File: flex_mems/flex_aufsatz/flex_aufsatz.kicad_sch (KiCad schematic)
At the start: 0 parts

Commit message: flex header first steps
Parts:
- added C6: 2.2uF, Capacitor_SMD:C_0402_1005Metric, symbol Device:C_Small
- added IC1: ADPL44002AUJZ-1.8-R7, ADPL44002AUJZ-1.8:SOT95P280X100-5N, symbol ADPL44002AUJZ-1.8:ADPL44002AUJZ-1.8-R7
- added J1, J2: Conn_01x22_Socket, Connector_PinSocket_2.54mm:PinSocket_1x22_P2.54mm_Vertical, symbol Connector:Conn_01x22_Socket
- added J3, J4: 10164228-0101A1RLF, header:AMPHENOL_10164228-0101A1RLF, symbol header:10164228-0101A1RLF
- added U1: ADAU7118ACPZRL, CP-16-22_ADI, symbol mux:ADAU7118ACPZRL
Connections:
- new net +1V8: C6.2, IC1.4 (SENSE/ADJ), IC1.5 (VOUT), U1.14 (DVDD)
- new net +3.3V: IC1.1 (VIN), IC1.3 (EN), J1.1 (Pin_1), U1.13 (EN), U1.16 (IOVDD)
- new net +3V3: J3.1, J4.1
- new net GND: C6.1, IC1.2 (GND), J1.22 (Pin_22), J3.10, J4.10, U1.15 (GND), U1.7 (SCL), U1.8 (SDA)
- new net MIC_CLK: J3.5, J4.4
- new net MIC_DOUT_0: J3.9
- new net MIC_DOUT_1: J3.7
- new net MIC_DOUT_2: J4.8
- no-connect marks 0 -> 11

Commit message: Schematics done
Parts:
- added C1, C2: 100nF, Capacitor_SMD:C_0402_1005Metric, symbol Device:C_Small
- added C3, C4: 2.2uF, Capacitor_SMD:C_0402_1005Metric, symbol Device:C_Small
- U1: footprint CP-16-22_ADI -> mux:QFN50P300X300X80-17N-D
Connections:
- net +3.3V: now also C1.1, C2.1, C3.1, C4.1
- net GND: now also J2.1 (Pin_1), U1.17 (EPAD), C1.2, C2.2, C3.2, C4.2
- net MIC_DOUT_0: now also U1.2 (PDM_DAT0)
- net MIC_DOUT_1: now also U1.3 (PDM_DAT1)
- net MIC_DOUT_2: now also U1.5 (PDM_DAT2)
- net TDM_DATA: now reaches J1.18 (Pin_18)
- net TDM_DATA: now also U1.11 (SDATA)
- net WS: now reaches J1.4 (Pin_4)
- net WS: now also U1.9 (FSYNC)
- net BCLK: now reaches J1.5 (Pin_5)
- net BCLK: now also U1.10 (BCLK)
- net MIC_CLK0: now reaches U1.1 (PDM_CLK0)
- net MIC_CLK0: now also J3.5
- net MIC_CLK1: now reaches U1.4 (PDM_CLK1)
- net MIC_CLK1: now also J4.4
- removed net MIC_CLK: J3.5, J4.4
- no-connect marks 11 -> 51

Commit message: flex_aufsatz1.0
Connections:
- net +3V3 is gone; now on net +3.3V: J3.1, J4.1
- net +3.3V: now also J1.2 (Pin_2)
- net GND: now also J2.21 (Pin_21), J2.22 (Pin_22)
- no-connect marks 51 -> 48
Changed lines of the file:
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@@
 	)
 	(junction
+		(at 35.56 29.21)
+		(diameter 0)
+		(color 0 0 0 0)
+	)
+	(junction
 		(at 266.7 44.45)
 		(diameter 0)
@@
 		(color 0 0 0 0)
 	)
+	(junction
+		(at 64.77 82.55)
+		(diameter 0)
+		(color 0 0 0 0)
+	)
 	(no_connect
 		(at 68.58 41.91)
@@
 	)
 	(no_connect
-		(at 68.58 82.55)
-	)
-	(no_connect
 		(at 68.58 67.31)
 	)
@@
 	)
 	(no_connect
-		(at 40.64 31.75)
-	)
-	(no_connect
 		(at 68.58 49.53)
 	)
@@
 	)
 	(no_connect
-		(at 68.58 80.01)
-	)
-	(no_connect
 		(at 68.58 62.23)
 	)
@@
 	(wire
 		(pts
+			(xy 64.77 82.55) (xy 68.58 82.55)
+		)
+		(stroke
+			(width 0)
+			(type default)
+		)
+	)
+	(wire
+		(pts
 			(xy 40.64 82.55) (xy 33.02 82.55)
 		)
@@
 	(wire
 		(pts
-			(xy 29.21 29.21) (xy 40.64 29.21)
+			(xy 29.21 29.21) (xy 35.56 29.21)
 		)
 		(stroke
@@
 	(wire
 		(pts
+			(xy 64.77 86.36) (xy 64.77 82.55)
+		)
+		(stroke
+			(width 0)
+			(type default)
+		)
+	)
+	(wire
+		(pts
 			(xy 274.32 44.45) (xy 274.32 49.53)
 		)
@@
 	(wire
 		(pts
+			(xy 64.77 80.01) (xy 64.77 82.55)
+		)
+		(stroke
+			(width 0)
+			(type default)
+		)
+	)
+	(wire
+		(pts
 			(xy 193.04 111.76) (xy 193.04 104.14)
 		)
@@
 	(wire
 		(pts
+			(xy 35.56 31.75) (xy 35.56 29.21)
+		)
+		(stroke
+			(width 0)
+			(type default)
+		)
+	)
+	(wire
+		(pts
 			(xy 81.28 119.38) (xy 90.17 119.38)
 		)
@@
 	(wire
 		(pts
+			(xy 40.64 31.75) (xy 35.56 31.75)
+		)
+		(stroke
+			(width 0)
+			(type default)
+		)
+	)
+	(wire
+		(pts
 			(xy 199.39 146.05) (xy 195.58 146.05)
 		)
@@
 	(wire
 		(pts
+			(xy 35.56 29.21) (xy 40.64 29.21)
+		)
+		(stroke
+			(width 0)
+			(type default)
+		)
+	)
+	(wire
+		(pts
 			(xy 90.17 127) (xy 90.17 129.54)
 		)
@@
 	(wire
 		(pts
+			(xy 68.58 80.01) (xy 64.77 80.01)
+		)
+		(stroke
+			(width 0)
+			(type default)
+		)
+	)
+	(wire
+		(pts
 			(xy 270.51 40.64) (xy 270.51 44.45)
 		)
@@
 	)
 	(symbol
+		(lib_id "power:GND")
+		(at 64.77 86.36 0)
+		(unit 1)
+		(exclude_from_sim no)
+		(in_bom yes)
+		(on_board yes)
+		(dnp no)
+		(fields_autoplaced yes)
+		(property "Reference" "#PWR015"
+			(at 64.77 92.71 0)
+			(effects
+				(font
+					(size 1.27 1.27)
+				)
+				(hide yes)
+			)
+		)
+		(property "Value" "GND"
+			(at 64.77 91.44 0)
+			(effects
+				(font
+					(size 1.27 1.27)
+				)
+			)
+		)
+		(property "Footprint" ""
+			(at 64.77 86.36 0)
+			(effects
+				(font
+					(size 1.27 1.27)
+				)
+				(hide yes)
+			)
+		)
+		(property "Datasheet" ""
+			(at 64.77 86.36 0)
+			(effects
+				(font
+					(size 1.27 1.27)
+				)
+				(hide yes)
+			)
+		)
+		(property "Description" "Power symbol creates a global label with name \"GND\" , ground"
+			(at 64.77 86.36 0)
+			(effects
+				(font
+					(size 1.27 1.27)
+				)
+				(hide yes)
+			)
+		)
+		(pin "1"
+		)
+		(instances
+			(project "flex_aufsatz"
+				(path "/1aeb6fc2-022e-4961-b0a7-a22f4026d221"
+					(reference "#PWR015")
+					(unit 1)
+				)
+			)
+		)
+	)
+	(symbol
 		(lib_id "Device:C_Small")
 		(at 26.67 25.4 270)
@@
 			)
 		)
-		(property "Value" "+3V3"
+		(property "Value" "+3.3V"
 			(at 193.04 100.33 0)
 			(effects
@@
 			)
 		)
-		(property "Value" "+3V3"
+		(property "Value" "+3.3V"
 			(at 195.58 134.62 0)
 			(effects

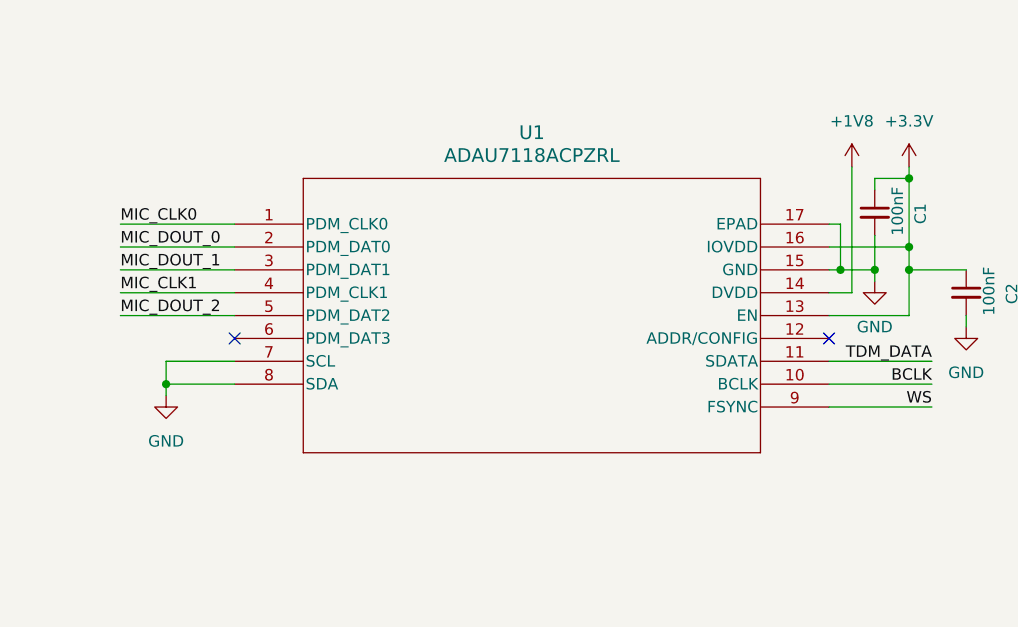
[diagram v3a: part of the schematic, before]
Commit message: GND zone update
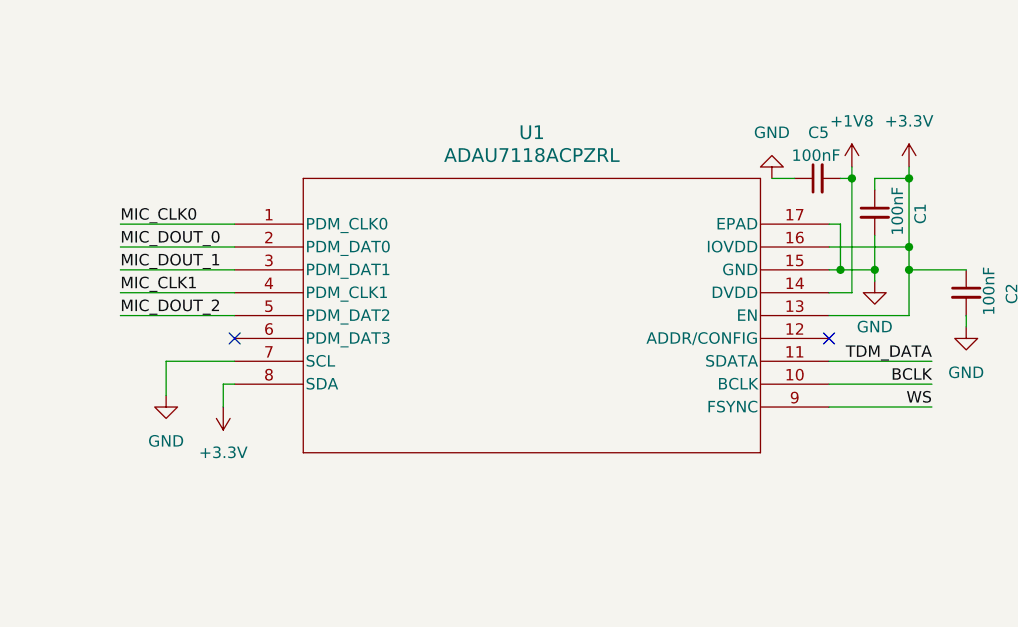
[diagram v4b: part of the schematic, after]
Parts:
- added C5: 100nF, Capacitor_SMD:C_0402_1005Metric, symbol Device:C_Small
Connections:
- net +1V8: now also C5.2
- net +3.3V: now also U1.8 (SDA)
- net GND: now also C5.1; no longer U1.8 (SDA)
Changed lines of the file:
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@@
 	)
 	(junction
-		(at 90.17 119.38)
+		(at 267.97 34.29)
 		(diameter 0)
 		(color 0 0 0 0)
 	)
 	(junction
-		(at 191.77 57.15)
+		(at 90.17 119.38)
 		(diameter 0)
 		(color 0 0 0 0)
@@
 	(wire
 		(pts
-			(xy 191.77 54.61) (xy 191.77 57.15)
+			(xy 186.69 39.37) (xy 199.39 39.37)
 		)
 		(stroke
@@
 	(wire
 		(pts
-			(xy 186.69 39.37) (xy 199.39 39.37)
+			(xy 64.77 82.55) (xy 68.58 82.55)
 		)
 		(stroke
@@
 	(wire
 		(pts
-			(xy 64.77 82.55) (xy 68.58 82.55)
+			(xy 40.64 82.55) (xy 33.02 82.55)
 		)
 		(stroke
@@
 	(wire
 		(pts
-			(xy 40.64 82.55) (xy 33.02 82.55)
+			(xy 265.43 39.37) (xy 266.7 39.37)
 		)
 		(stroke
@@
 	(wire
 		(pts
-			(xy 265.43 39.37) (xy 266.7 39.37)
+			(xy 224.79 148.59) (xy 236.22 148.59)
 		)
 		(stroke
@@
 	(wire
 		(pts
-			(xy 224.79 148.59) (xy 236.22 148.59)
+			(xy 199.39 57.15) (xy 198.12 57.15)
 		)
 		(stroke
@@
 	(wire
 		(pts
+			(xy 267.97 34.29) (xy 267.97 33.02)
+		)
+		(stroke
+			(width 0)
+			(type default)
+		)
+	)
+	(wire
+		(pts
 			(xy 265.43 57.15) (xy 276.86 57.15)
 		)
@@
 	(wire
 		(pts
+			(xy 198.12 57.15) (xy 198.12 59.69)
+		)
+		(stroke
+			(width 0)
+			(type default)
+		)
+	)
+	(wire
+		(pts
 			(xy 228.6 157.48) (xy 228.6 158.75)
 		)
@@
 	(wire
 		(pts
-			(xy 191.77 57.15) (xy 191.77 58.42)
+			(xy 191.77 54.61) (xy 191.77 58.42)
 		)
 		(stroke
@@
 	(wire
 		(pts
+			(xy 266.7 34.29) (xy 267.97 34.29)
+		)
+		(stroke
+			(width 0)
+			(type default)
+		)
+	)
+	(wire
+		(pts
 			(xy 30.48 72.39) (xy 40.64 72.39)
 		)
@@
 	(wire
 		(pts
-			(xy 267.97 46.99) (xy 267.97 33.02)
+			(xy 267.97 46.99) (xy 267.97 34.29)
 		)
 		(stroke
@@
 	(wire
 		(pts
+			(xy 259.08 34.29) (xy 261.62 34.29)
+		)
+		(stroke
+			(width 0)
+			(type default)
+		)
+	)
+	(wire
+		(pts
 			(xy 64.77 31.75) (xy 64.77 29.21)
 		)
@@
 	(wire
 		(pts
-			(xy 191.77 57.15) (xy 199.39 57.15)
-		)
-		(stroke
-			(width 0)
-			(type default)
-		)
-	)
-	(wire
-		(pts
 			(xy 226.06 121.92) (xy 226.06 123.19)
 		)
@@
 	)
 	(symbol
+		(lib_id "power:+3.3V")
+		(at 198.12 59.69 180)
+		(unit 1)
+		(exclude_from_sim no)
+		(in_bom yes)
+		(on_board yes)
+		(dnp no)
+		(fields_autoplaced yes)
+		(property "Reference" "#PWR016"
+			(at 198.12 55.88 0)
+			(effects
+				(font
+					(size 1.27 1.27)
+				)
+				(hide yes)
+			)
+		)
+		(property "Value" "+3.3V"
+			(at 198.12 64.77 0)
+			(effects
+				(font
+					(size 1.27 1.27)
+				)
+			)
+		)
+		(property "Footprint" ""
+			(at 198.12 59.69 0)
+			(effects
+				(font
+					(size 1.27 1.27)
+				)
+				(hide yes)
+			)
+		)
+		(property "Datasheet" ""
+			(at 198.12 59.69 0)
+			(effects
+				(font
+					(size 1.27 1.27)
+				)
+				(hide yes)
+			)
+		)
+		(property "Description" "Power symbol creates a global label with name \"+3.3V\""
+			(at 198.12 59.69 0)
+			(effects
+				(font
+					(size 1.27 1.27)
+				)
+				(hide yes)
+			)
+		)
+		(pin "1"
+		)
+		(instances
+			(project "flex_aufsatz"
+				(path "/1aeb6fc2-022e-4961-b0a7-a22f4026d221"
+					(reference "#PWR016")
+					(unit 1)
+				)
+			)
+		)
+	)
+	(symbol
 		(lib_id "Connector:Conn_01x22_Socket")
 		(at 45.72 54.61 0)
@@
 	)
 	(symbol
+		(lib_id "power:GND")
+		(at 259.08 34.29 180)
+		(unit 1)
+		(exclude_from_sim no)
+		(in_bom yes)
+		(on_board yes)
+		(dnp no)
+		(fields_autoplaced yes)
+		(property "Reference" "#PWR019"
+			(at 259.08 27.94 0)
+			(effects
+				(font
+					(size 1.27 1.27)
+				)
+				(hide yes)
+			)
+		)
+		(property "Value" "GND"
+			(at 259.08 29.21 0)
+			(effects
+				(font
+					(size 1.27 1.27)
+				)
+			)
+		)
+		(property "Footprint" ""
+			(at 259.08 34.29 0)
+			(effects
+				(font
+					(size 1.27 1.27)
+				)
+				(hide yes)
+			)
+		)
+		(property "Datasheet" ""
+			(at 259.08 34.29 0)
+			(effects
+				(font
+					(size 1.27 1.27)
+				)
+				(hide yes)
+			)
+		)
+		(property "Description" "Power symbol creates a global label with name \"GND\" , ground"
+			(at 259.08 34.29 0)
+			(effects
+				(font
+					(size 1.27 1.27)
+				)
+				(hide yes)
+			)
+		)
+		(pin "1"
+		)
+		(instances
+			(project "flex_aufsatz"
+				(path "/1aeb6fc2-022e-4961-b0a7-a22f4026d221"
+					(reference "#PWR019")
+					(unit 1)
+				)
+			)
+		)
+	)
+	(symbol
 		(lib_id "Device:C_Small")
 		(at 270.51 38.1 0)
@@
 					(unit 1)
 				)
+			)
+		)
+	)
+	(symbol
+		(lib_id "Device:C_Small")
+		(at 264.16 34.29 90)
+		(unit 1)
+		(exclude_from_sim no)
+		(in_bom yes)
+		(on_board yes)
+		(dnp no)
+		(property "Reference" "C5"
+			(at 265.43 29.21 90)
+			(effects
+				(font
+					(size 1.27 1.27)
+				)
+				(justify left)
+			)
+		)
+		(property "Value" "100nF"
+			(at 266.7 31.75 90)
+			(effects
+				(font
+					(size 1.27 1.27)
+				)
+				(justify left)
+			)
+		)
+		(property "Footprint" "Capacitor_SMD:C_0402_1005Metric"
+			(at 264.16 34.29 0)
+			(effects
+				(font
+					(size 1.27 1.27)
+				)
+				(hide yes)
+			)
+		)
+		(property "Datasheet" "~"
+			(at 264.16 34.29 0)
+			(effects
+				(font
+					(size 1.27 1.27)
+				)
+				(hide yes)
+			)
+		)
+		(property "Description" ""
+			(at 264.16 34.29 0)
+			(effects
+				(font
+					(size 1.27 1.27)
+				)
+				(hide yes)
+			)
+		)
+		(pin "1"
+		)
+		(pin "2"
+		)
+		(instances
+			(project "flex_aufsatz"
+				(path "/1aeb6fc2-022e-4961-b0a7-a22f4026d221"
+					(reference "C5")
+					(unit 1)
+				)
